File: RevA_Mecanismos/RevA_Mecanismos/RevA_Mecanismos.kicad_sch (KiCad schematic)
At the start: 29 parts, among them J1 PROG, J17 Conn_01x02_Socket, Q2 AO3400A, SW1 SW_Push, U1 STM32L431RCTx, Y1 16MHz

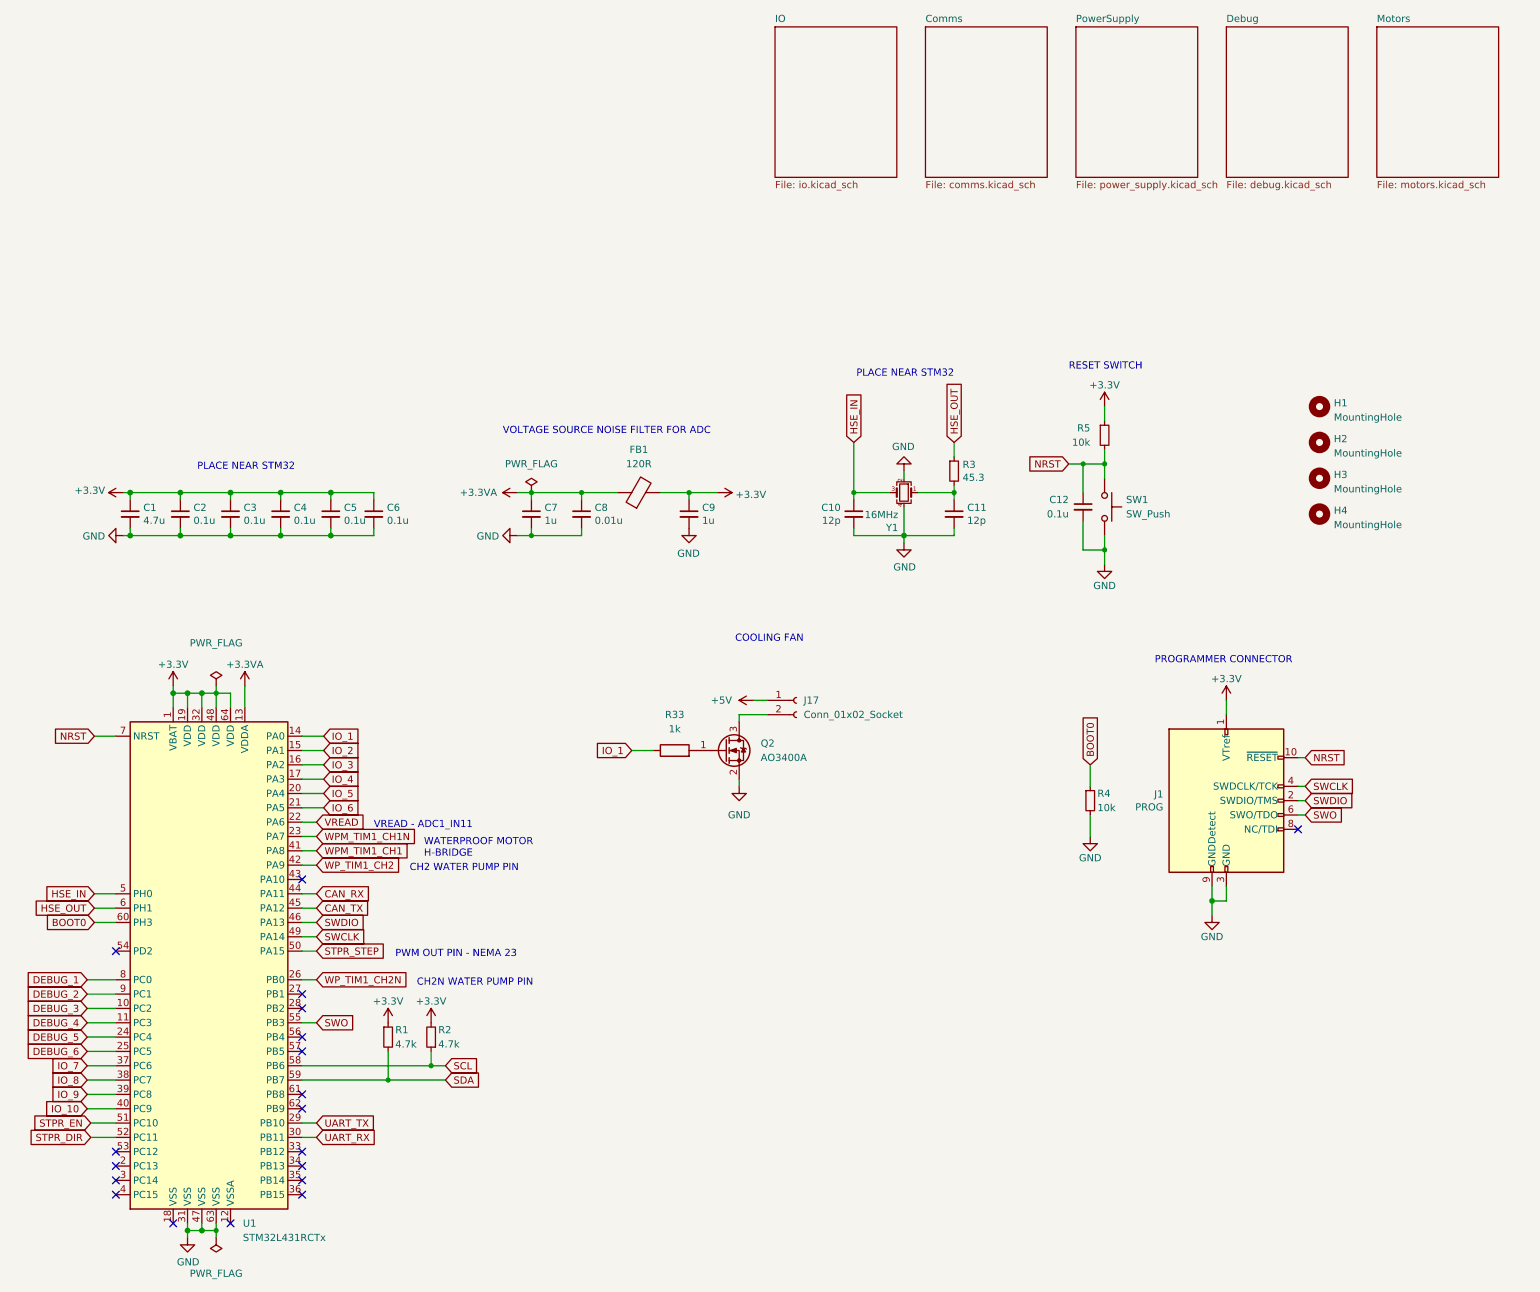
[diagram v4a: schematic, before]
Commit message: Updated STM32 USV Mechanism PCB
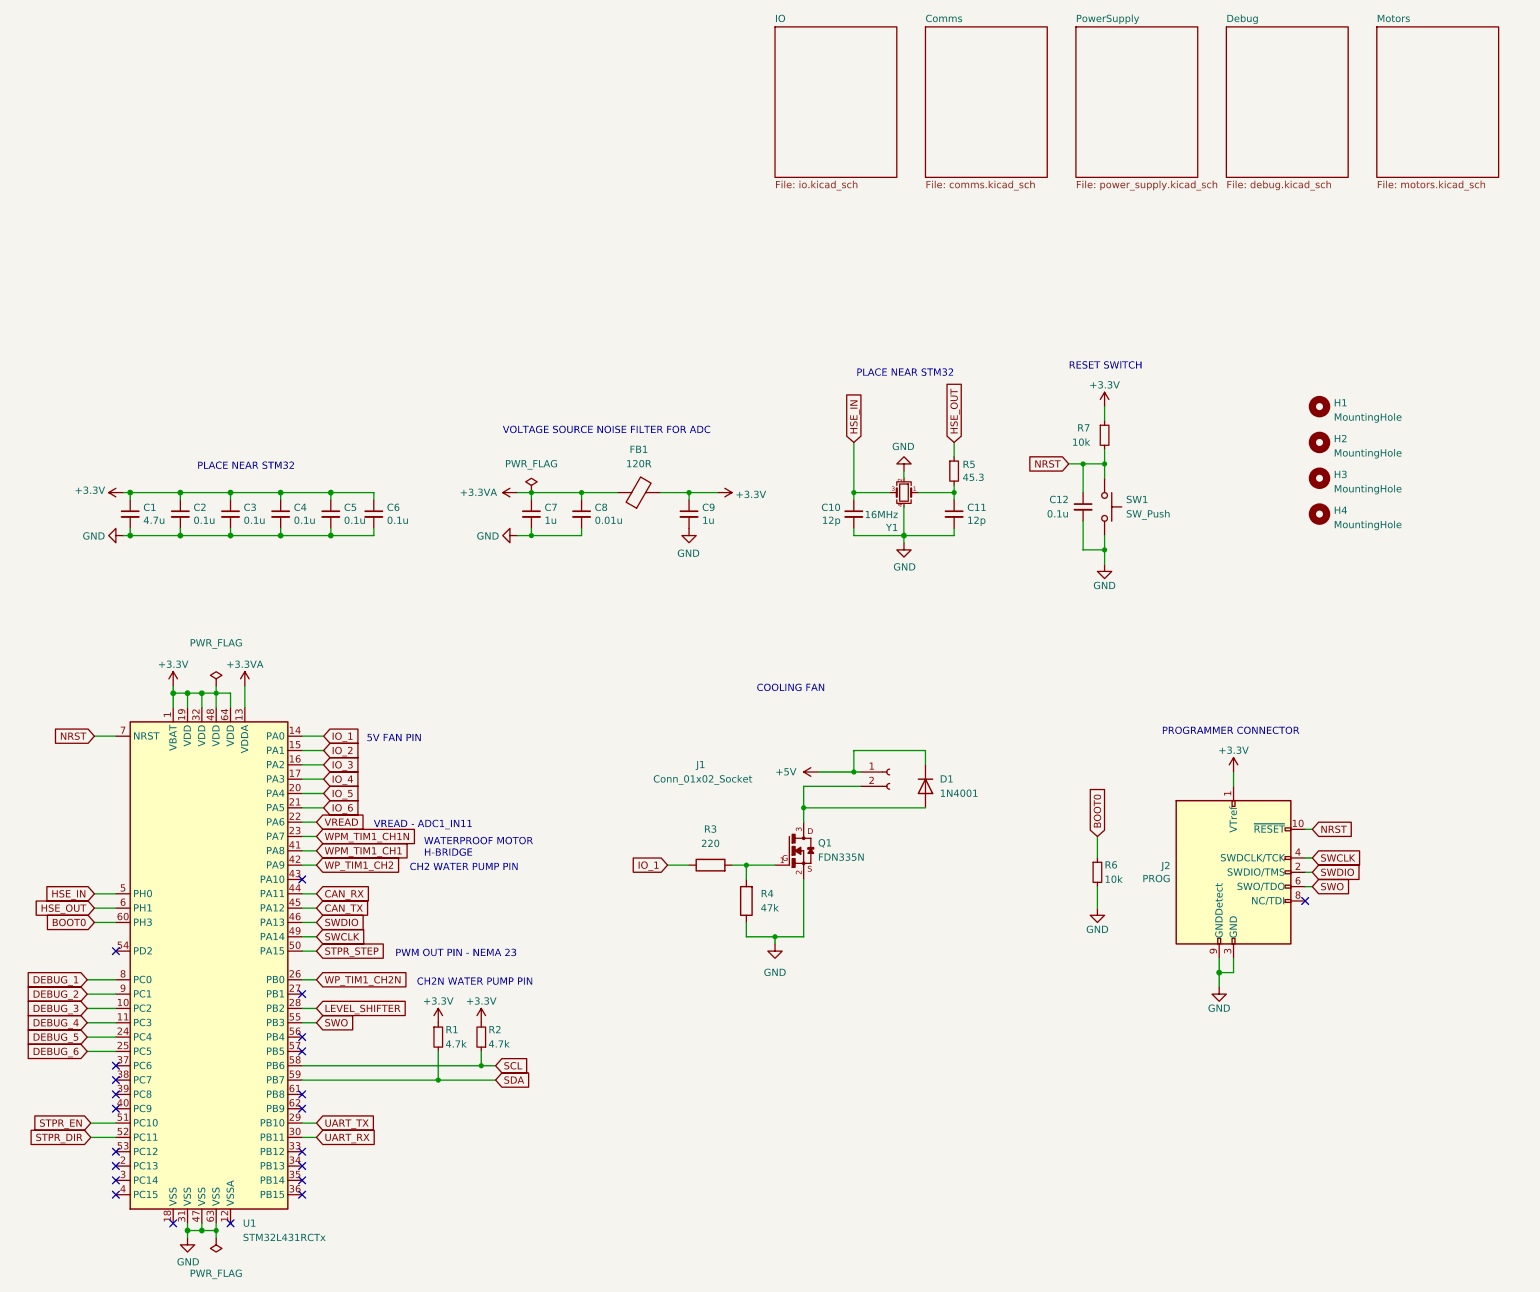
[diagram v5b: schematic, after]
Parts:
- removed J17: Conn_01x02_Socket, Connector_PinHeader_2.54mm:PinHeader_1x02_P2.54mm_Vertical, symbol Connector:Conn_01x02_Socket
- removed Q2: AO3400A, Package_TO_SOT_SMD:SOT-23, symbol Transistor_FET:AO3400A
- removed R33: 1k, symbol Device:R
- added D1: 1N4001, Diode_THT:D_DO-41_SOD81_P10.16mm_Horizontal, symbol Diode:1N4001
- added J1: Conn_01x02_Socket, Connector_PinHeader_2.54mm:PinHeader_1x02_P2.54mm_Vertical, symbol Connector:Conn_01x02_Socket
- added Q1: FDN335N, FDN335N:SSOT-3, symbol FDN335N:FDN335N
- added R3: 220, Resistor_SMD:R_0603_1608Metric, symbol Device:R
- added R4: 47k, Resistor_SMD:R_0603_1608Metric, symbol Device:R
- renumbered J1 to J2, R3 to R5, R4 to R6, R5 to R7
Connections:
- net +5V: now also D1.1 (K), J1.1 (Pin_1)
- net GND: now also Q1.2, R4.1
- net IO_1: now also R3.1
- net LEVEL_SHIFTER: now reaches U1.28 (PB2)
- net IO_10: no longer names the net of U1.40 (PC9)
- net IO_7: no longer names the net of U1.37 (PC6)
- net IO_8: no longer names the net of U1.38 (PC7)
- net IO_9: no longer names the net of U1.39 (PC8)
- new net: D1.2 (A), J1.2 (Pin_2), Q1.3
- new net: Q1.1, R3.2, R4.2
- no-connect marks 19 -> 22
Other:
- note added: "5V FAN PIN"
- moved on the sheet: J2, R1, R2, R6

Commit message: Complete schematic and pcb designs, routes missing and not yet complete
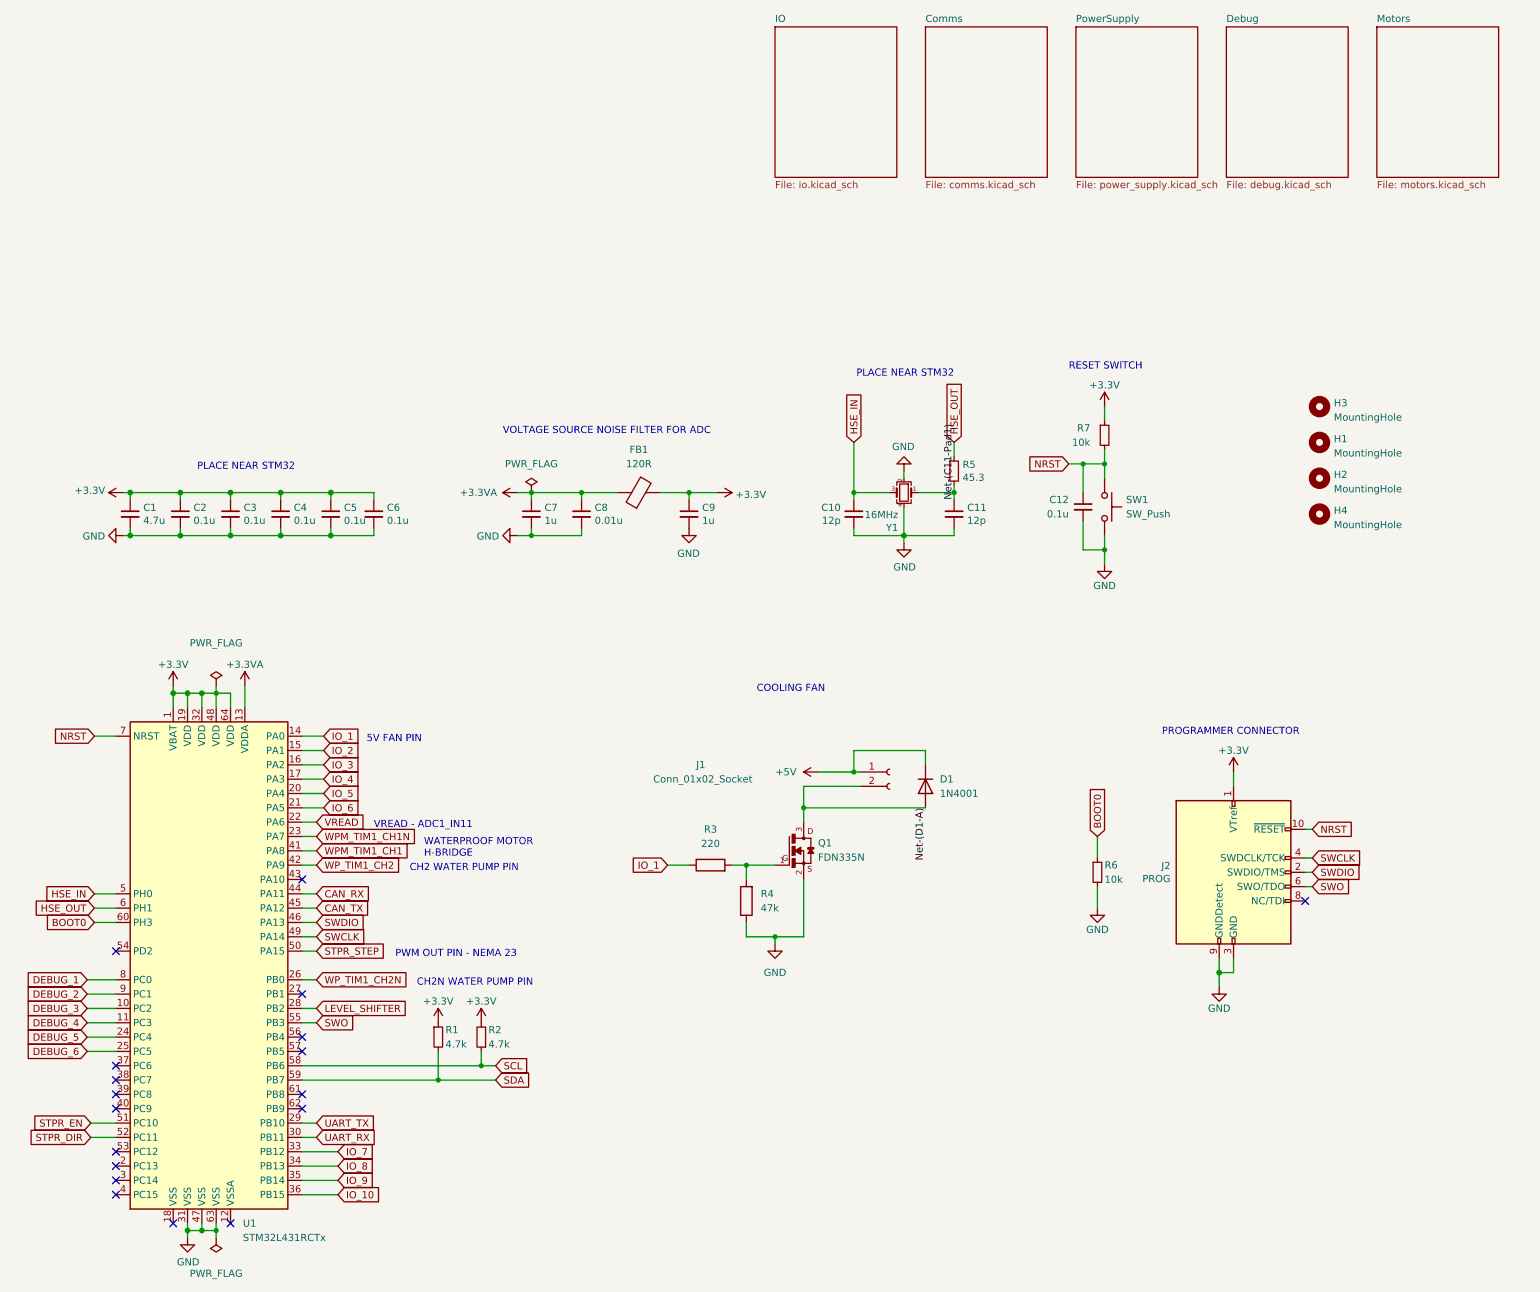
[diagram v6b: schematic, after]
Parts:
- renumbered H2 to H1, H3 to H2, H1 to H3
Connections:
- net Net-(D1-A): now reaches D1.2 (A), J1.2 (Pin_2), Q1.3
- net Net-(C11-Pad1): now reaches C11.1, R5.2, Y1.1
- net IO_7: now reaches U1.33 (PB12)
- net IO_8: now reaches U1.34 (PB13)
- net IO_9: now reaches U1.35 (PB14)
- net IO_10: now reaches U1.36 (PB15)
- no-connect marks 22 -> 18
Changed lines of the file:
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@@
   (no_connect (at 73.66 160.02))
   (no_connect (at 40.64 132.08))
-  (no_connect (at 73.66 172.72))
   (no_connect (at 40.64 152.4))
   (no_connect (at 40.64 160.02))
@@
   (no_connect (at 60.96 180.34))
   (no_connect (at 73.66 157.48))
-  (no_connect (at 73.66 170.18))
   (no_connect (at 73.66 139.7))
   (no_connect (at 40.64 172.72))
   (no_connect (at 73.66 119.38))
-  (no_connect (at 73.66 175.26))
-  (no_connect (at 73.66 167.64))
   (no_connect (at 73.66 149.86))
   (wire (pts (xy 212.09 45.72) (xy 212.09 50.8))
@@
     (stroke (width 0) (type default))
   )
+  (wire (pts (xy 73.66 175.26) (xy 80.01 175.26))
+    (stroke (width 0) (type default))
+  )
   (wire (pts (xy 35.56 142.24) (xy 40.64 142.24))
     (stroke (width 0) (type default))
@@
     (stroke (width 0) (type solid))
   )
+  (wire (pts (xy 73.66 172.72) (xy 80.01 172.72))
+    (stroke (width 0) (type default))
+  )
   (wire (pts (xy 215.9 58.42) (xy 215.9 60.96))
     (stroke (width 0) (type default))
@@
     (stroke (width 0) (type solid))
   )
+  (wire (pts (xy 73.66 167.64) (xy 80.01 167.64))
+    (stroke (width 0) (type default))
+  )
   (wire (pts (xy 58.42 86.36) (xy 60.96 86.36))
     (stroke (width 0) (type default))
@@
   )
   (wire (pts (xy 73.66 127) (xy 76.2 127))
+    (stroke (width 0) (type default))
+  )
+  (wire (pts (xy 73.66 170.18) (xy 80.01 170.18))
     (stroke (width 0) (type default))
   )
@@
   (text "WATERPROOF MOTOR\nH-BRIDGE" (at 95.25 115.57 0)
     (effects (font (size 1.27 1.27)) (justify left bottom))
+  )
+  (label "Net-(C11-Pad1)" (at 189.23 52.07 90) (fields_autoplaced)
+    (effects (font (size 1.27 1.27)) (justify left bottom))
+  )
+  (label "Net-(D1-A)" (at 184.15 106.68 270) (fields_autoplaced)
+    (effects (font (size 1.27 1.27)) (justify right bottom))
   )
   (global_label "IO_6" (shape input) (at 77.47 106.68 0)
@@
     )
   )
+  (global_label "IO_10" (shape input) (at 80.01 175.26 0)
+    (effects (font (size 1.27 1.27)) (justify left))
+    (property "Intersheetrefs" "${INTERSHEET_REFS}" (at 88.7247 175.3394 0)
+      (effects (font (size 1.27 1.27)) (justify left) hide)
+    )
+  )
   (global_label "SWO" (shape input) (at 252.73 120.65 0)
     (effects (font (size 1.27 1.27)) (justify left))
@@
     (effects (font (size 1.27 1.27)) (justify left))
     (property "Intersheetrefs" "${INTERSHEET_REFS}" (at 86.7169 165.0206 0)
+      (effects (font (size 1.27 1.27)) (justify left) hide)
+    )
+  )
+  (global_label "IO_9" (shape input) (at 80.01 172.72 0)
+    (effects (font (size 1.27 1.27)) (justify left))
+    (property "Intersheetrefs" "${INTERSHEET_REFS}" (at 88.7247 172.7994 0)
       (effects (font (size 1.27 1.27)) (justify left) hide)
     )
@@
     )
   )
+  (global_label "IO_8" (shape input) (at 80.01 170.18 0)
+    (effects (font (size 1.27 1.27)) (justify left))
+    (property "Intersheetrefs" "${INTERSHEET_REFS}" (at 88.7247 170.2594 0)
+      (effects (font (size 1.27 1.27)) (justify left) hide)
+    )
+  )
   (global_label "DEBUG_1" (shape input) (at 35.56 137.16 180)
     (effects (font (size 1.27 1.27)) (justify right))
@@
     (effects (font (size 1.27 1.27)) (justify left))
     (property "Intersheetrefs" "${INTERSHEET_REFS}" (at 87.2733 116.9194 0)
+      (effects (font (size 1.27 1.27)) (justify left) hide)
+    )
+  )
+  (global_label "IO_7" (shape input) (at 80.01 167.64 0)
+    (effects (font (size 1.27 1.27)) (justify left))
+    (property "Intersheetrefs" "${INTERSHEET_REFS}" (at 88.7247 167.7194 0)
       (effects (font (size 1.27 1.27)) (justify left) hide)
     )
@@
   (symbol (lib_id "Mechanical:MountingHole") (at 254 35.56 0) (unit 1)
     (in_bom yes) (on_board yes) (dnp no) (fields_autoplaced)
-    (property "Reference" "H1" (at 256.54 34.925 0)
+    (property "Reference" "H3" (at 256.54 34.925 0)
       (effects (font (size 1.27 1.27)) (justify left))
     )
@@
       (project "RevA_Mecanismos"
         (path "/3a16a434-10b7-49a8-988b-273362cb395e"
-          (reference "H1") (unit 1)
+          (reference "H3") (unit 1)
         )
       )
@@
   (symbol (lib_id "Mechanical:MountingHole") (at 254 48.26 0) (unit 1)
     (in_bom yes) (on_board yes) (dnp no) (fields_autoplaced)
-    (property "Reference" "H3" (at 256.54 47.625 0)
+    (property "Reference" "H2" (at 256.54 47.625 0)
       (effects (font (size 1.27 1.27)) (justify left))
     )
@@
       (project "RevA_Mecanismos"
         (path "/3a16a434-10b7-49a8-988b-273362cb395e"
-          (reference "H3") (unit 1)
+          (reference "H2") (unit 1)
         )
       )
@@
   (symbol (lib_id "Mechanical:MountingHole") (at 254 41.91 0) (unit 1)
     (in_bom yes) (on_board yes) (dnp no) (fields_autoplaced)
-    (property "Reference" "H2" (at 256.54 41.275 0)
+    (property "Reference" "H1" (at 256.54 41.275 0)
       (effects (font (size 1.27 1.27)) (justify left))
     )
@@
       (project "RevA_Mecanismos"
         (path "/3a16a434-10b7-49a8-988b-273362cb395e"
-          (reference "H2") (unit 1)
-        )
-      )
+          (reference "H1") (unit 1)
+        )
+      )
